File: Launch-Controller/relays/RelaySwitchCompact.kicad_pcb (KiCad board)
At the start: 2 copper layers, 38.2 x 17 mm, 13 parts, among them J1 Conn_01x05_Pin, K1 1-1721150-0, U1 FOD817ASD, U2 FMMT634QTA

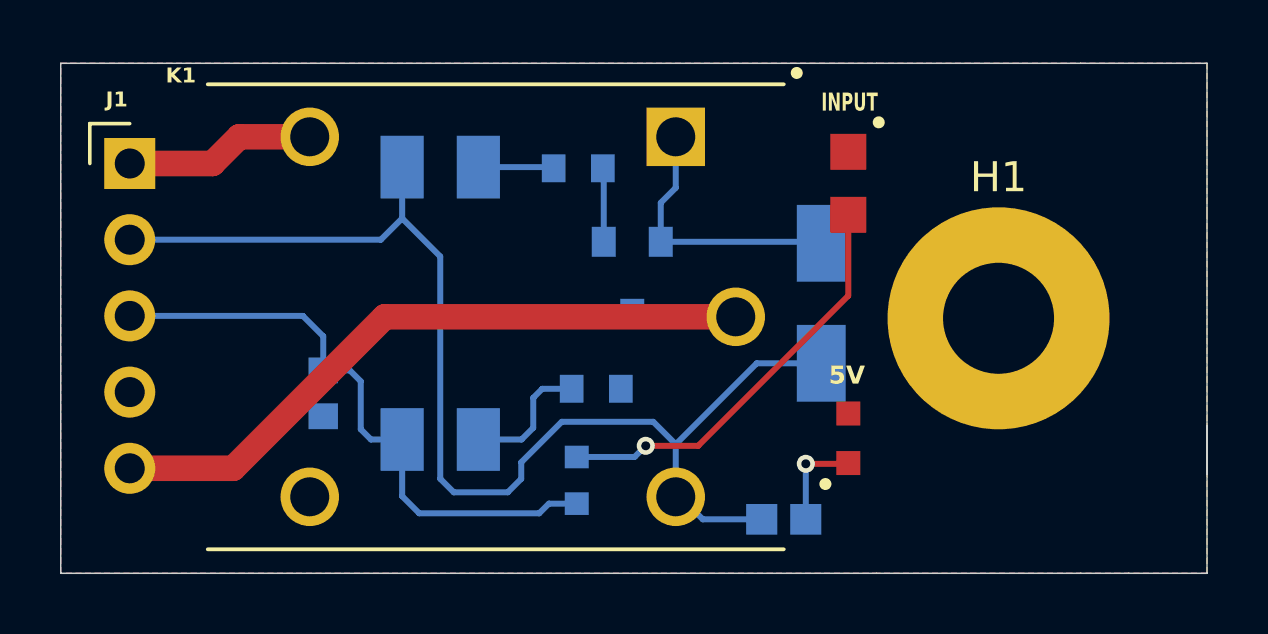
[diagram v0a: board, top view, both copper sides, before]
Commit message: fized relay
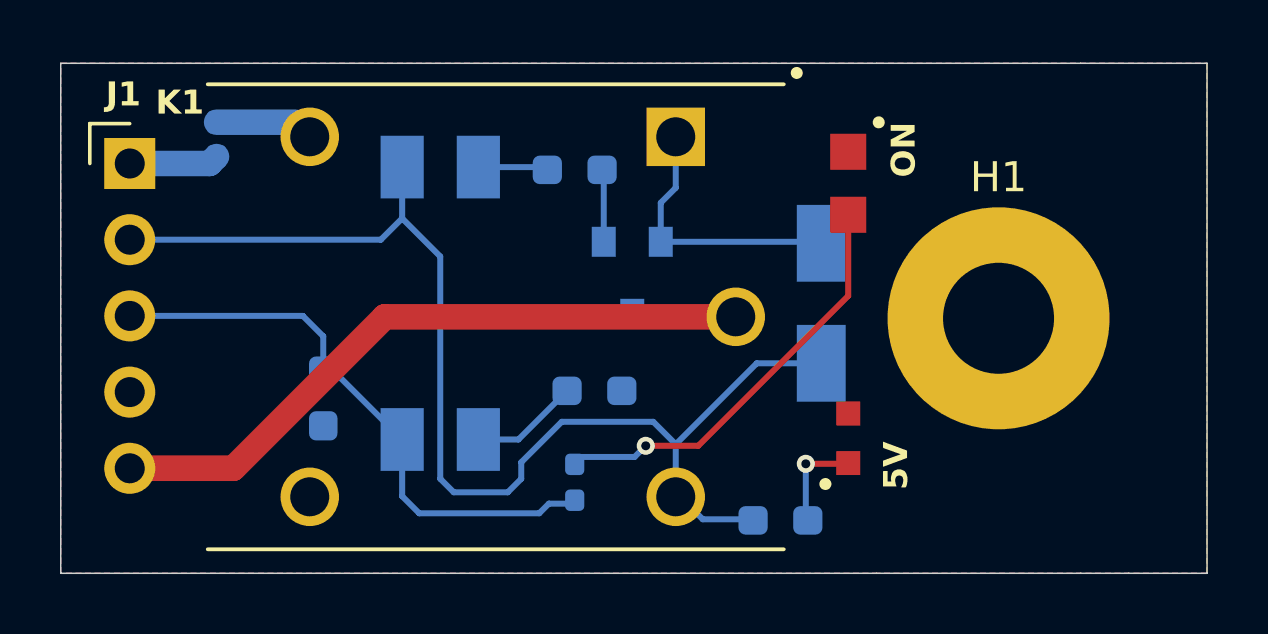
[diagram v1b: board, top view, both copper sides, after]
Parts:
- removed REF**: RC0603N_PAN, footprints68R:RC0603N_PAN
- added F1: Fuse, Diode_SMD:D_0402_1005Metric_Pad0.77x0.64mm_HandSolder, B.Cu at (155.2, 97.5)
- added R5: 100R, Resistor_SMD:R_0603_1608Metric_Pad0.98x0.95mm_HandSolder, B.Cu at (167.1, 98.6)
- R1: value 330R -> 68R; footprint RC0603FR-07330RL:RESC1607X60N -> Resistor_SMD:R_0402_1005Metric_Pad0.72x0.64mm_HandSolder; moved to B.Cu
- R2: value 100R -> 10k; footprint AC0603JR-07100RL:RESC1608X55N -> Resistor_SMD:R_0603_1608Metric_Pad0.98x0.95mm_HandSolder; moved to B.Cu
- R3: footprint AC0603JR-07100RL:RESC1608X55N -> Resistor_SMD:R_0603_1608Metric_Pad0.98x0.95mm_HandSolder; moved to B.Cu
- R4: value 10k -> 330R; footprint CRCW060310K0DHEAP:RESC1508X50N -> Resistor_SMD:R_0603_1608Metric_Pad0.98x0.95mm_HandSolder; moved to B.Cu
- moved R4 15.8 mm to (174.0, 110.2), turned to 180 degrees
- moved R2 11.5 mm to (158.8, 106.2), turned to 90 degrees
- moved R1 7.08 mm to (167.1, 109.0), turned to -90 degrees
- moved R3 0.09 mm to (167.8, 105.9)
- renumbered LED2 to LED1, LED1 to LED2
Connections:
- K1 pad 5: /RelayIn -> Net-(F1-Pad2)
- LED1 pad A: Net-(LED2-PadA) -> Net-(LED1-PadA)
- LED1 pad C: /GND -> GND
- LED2 pad 1: /GND -> GND
- LED2 pad 2: Net-(LED1-A) -> Net-(LED2-A)
- R1 pad 1: Net-(LED1-A) -> Net-(LED1-PadA)
- R1 pad 2: /+5V -> /GPIO
- R2 pad 1: Net-(R2-Pad1) -> GND
- R2 pad 2: Net-(U2-B) -> /GPIO
- R4 pad 1: /GND -> Net-(LED2-A)
- R4 pad 2: /GPIO -> +5V
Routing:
- net /+5V: track 40.8 -> 0.00 mm
- net +5V: track 0.00 -> 40.8 mm
- net Net-(LED2-PadA): track 14.0 -> 0.00 mm, vias 1 -> 0
- net Net-(LED1-PadA): track 0.00 -> 13.8 mm, vias 0 -> 1
- net /RelayIn: track 6.37 -> 2.99 mm
- net Net-(F1-Pad2): track 0.00 -> 3.31 mm
- net Net-(LED2-A): track 0.00 -> 3.28 mm, vias 0 -> 1
- net Net-(LED1-A): track 3.28 -> 0.00 mm, vias 1 -> 0
- net Net-(R5-Pad1): track 0.00 -> 2.53 mm
- net Net-(R2-Pad1): track 2.53 -> 0.00 mm
- net /GPIO: track 20.6 -> 19.5 mm
- net Net-(R3-Pad2): track 4.40 -> 3.63 mm
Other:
- outline, holes or cut-outs redrawn
- board text added: "ON"
- board text removed: "INPUT"
- board text removed: "R1"
- board text removed: "R2"
- board text removed: "R3"
- board text removed: "R5"

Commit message: more relay changes
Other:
- board text removed: "R4"
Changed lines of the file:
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@@
 		(tags "resistor handsolder")
 		(property "Reference" "R2"
-			(at 0 1.43 90)
+			(at 0 -1.27 90)
 			(layer "B.SilkS")
 			(effects
 				(font
-					(size 1 1)
+					(size 0.8 0.8)
 					(thickness 0.15)
 				)
@@
 		(tags "resistor handsolder")
 		(property "Reference" "R1"
-			(at 0 1.17 90)
+			(at 0 1.016 90)
 			(layer "B.SilkS")
 			(effects
 				(font
-					(size 1 1)
+					(size 0.8 0.8)
 					(thickness 0.15)
 				)
@@
 		(tags "resistor handsolder")
 		(property "Reference" "R5"
-			(at 0 1.43 360)
+			(at 0 -1.27 0)
 			(layer "B.SilkS")
 			(effects
 				(font
-					(size 1 1)
+					(size 0.8 0.8)
 					(thickness 0.15)
 				)
@@
 		(tags "resistor handsolder")
 		(property "Reference" "R3"
-			(at 0 1.43 360)
+			(at -2.6435 0 0)
 			(layer "B.SilkS")
 			(effects
 				(font
-					(size 1 1)
+					(size 0.8 0.8)
 					(thickness 0.15)
 				)
@@
 		(tags "resistor handsolder")
 		(property "Reference" "R4"
-			(at 0 1.43 360)
+			(at 0 1.43 0)
 			(layer "B.SilkS")
 			(effects
 				(font
-					(size 1 1)
+					(size 0.8 0.8)
 					(thickness 0.15)
 				)
@@
 		)
 	)
-	(gr_text "R4"
-		(at 158 106.2 0)
-		(layer "B.SilkS")
-		(effects
-			(font
-				(size 0.8 0.8)
-				(thickness 0.1)
-				(bold yes)
-			)
-			(justify left bottom mirror)
-		)
-	)
 	(gr_text "D1"
 		(at 174.1 106.725 0)
@@
 	)
 	(gr_text "U1"
-		(at 163 96.85 0)
+		(at 163.576 96.85 0)
 		(layer "B.SilkS")
 		(effects
@@
 		(members "2886e332-e9b1-4839-b927-1127fd8a52fa" "eb389d97-817e-4d49-a7a3-42364710dffd")
 	)
-	(group ""
-		(members "6ad9c6ec-2604-4079-9361-f6d3650d4035")
-	)
 )
